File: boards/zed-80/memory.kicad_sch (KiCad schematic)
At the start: 6 parts, among them U3 TT74LS32BI, U5 AT28C256-15PU, U7 HM628128BLP-10

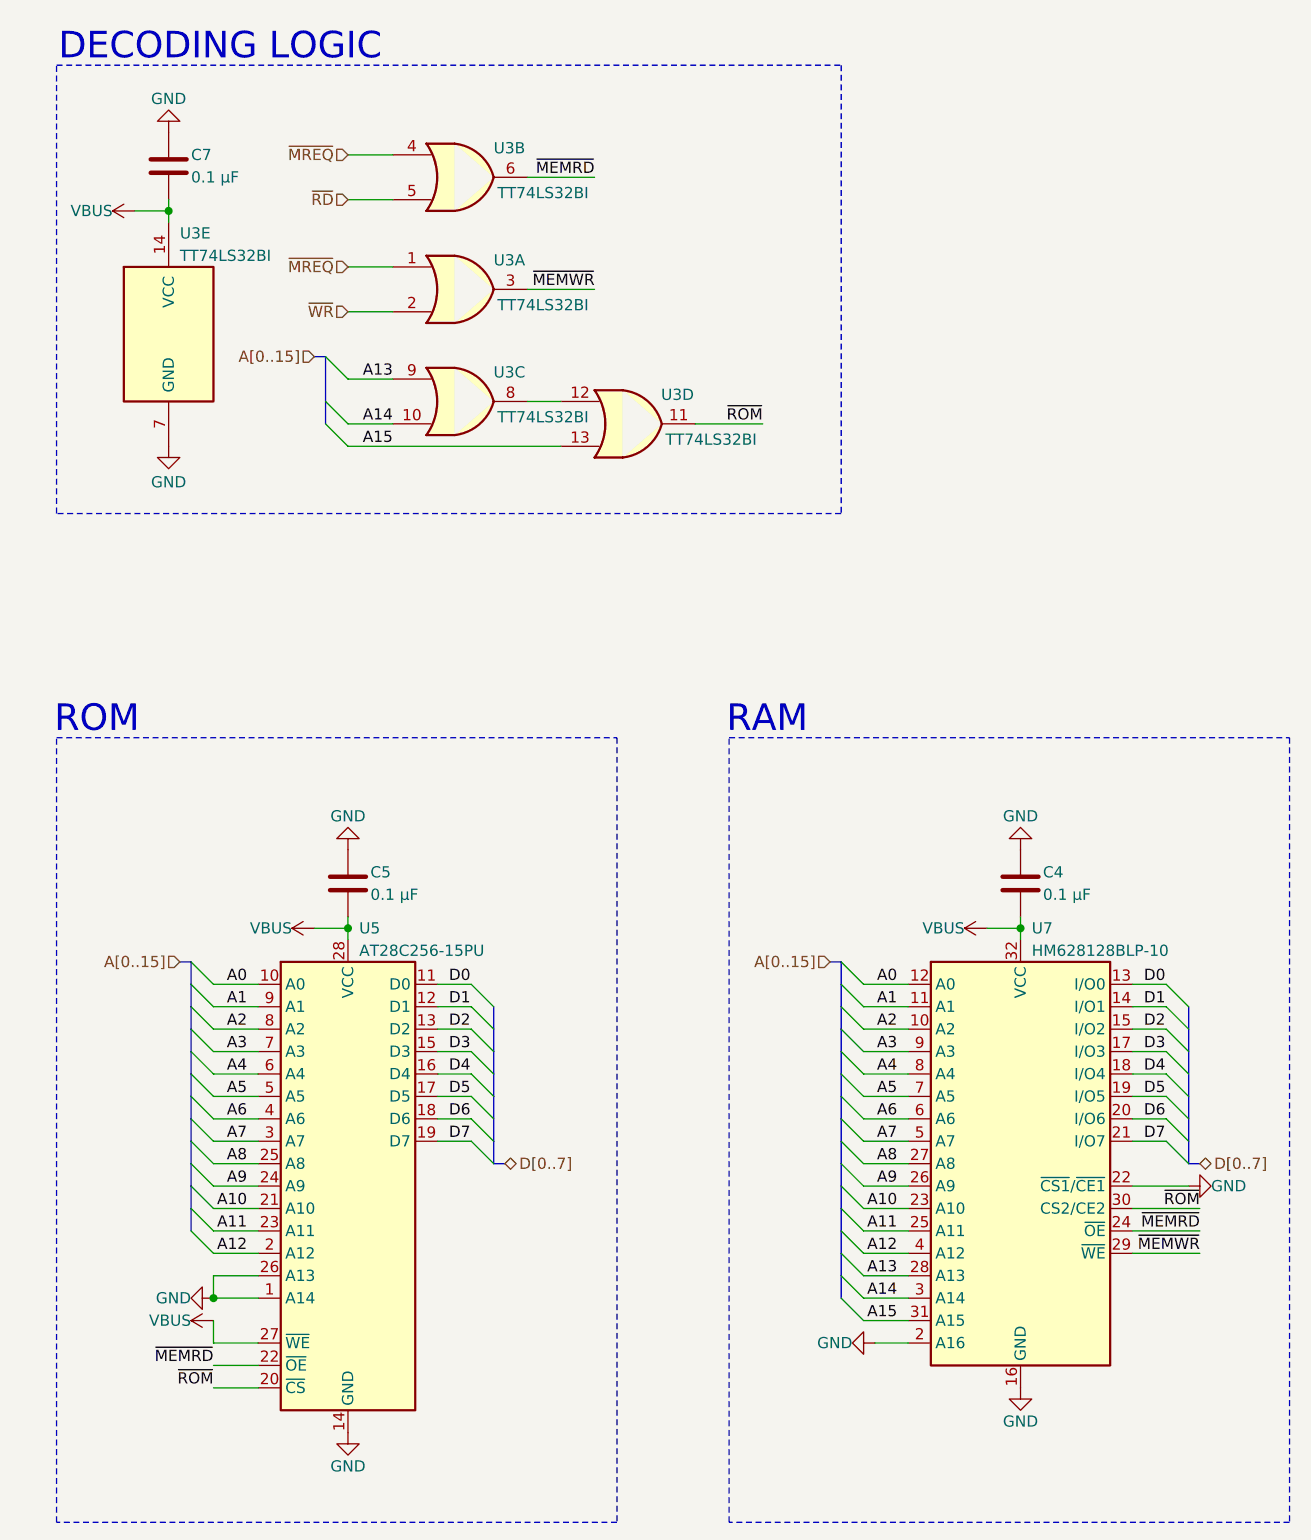
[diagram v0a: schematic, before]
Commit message: Polished schematics and basic PCB setup
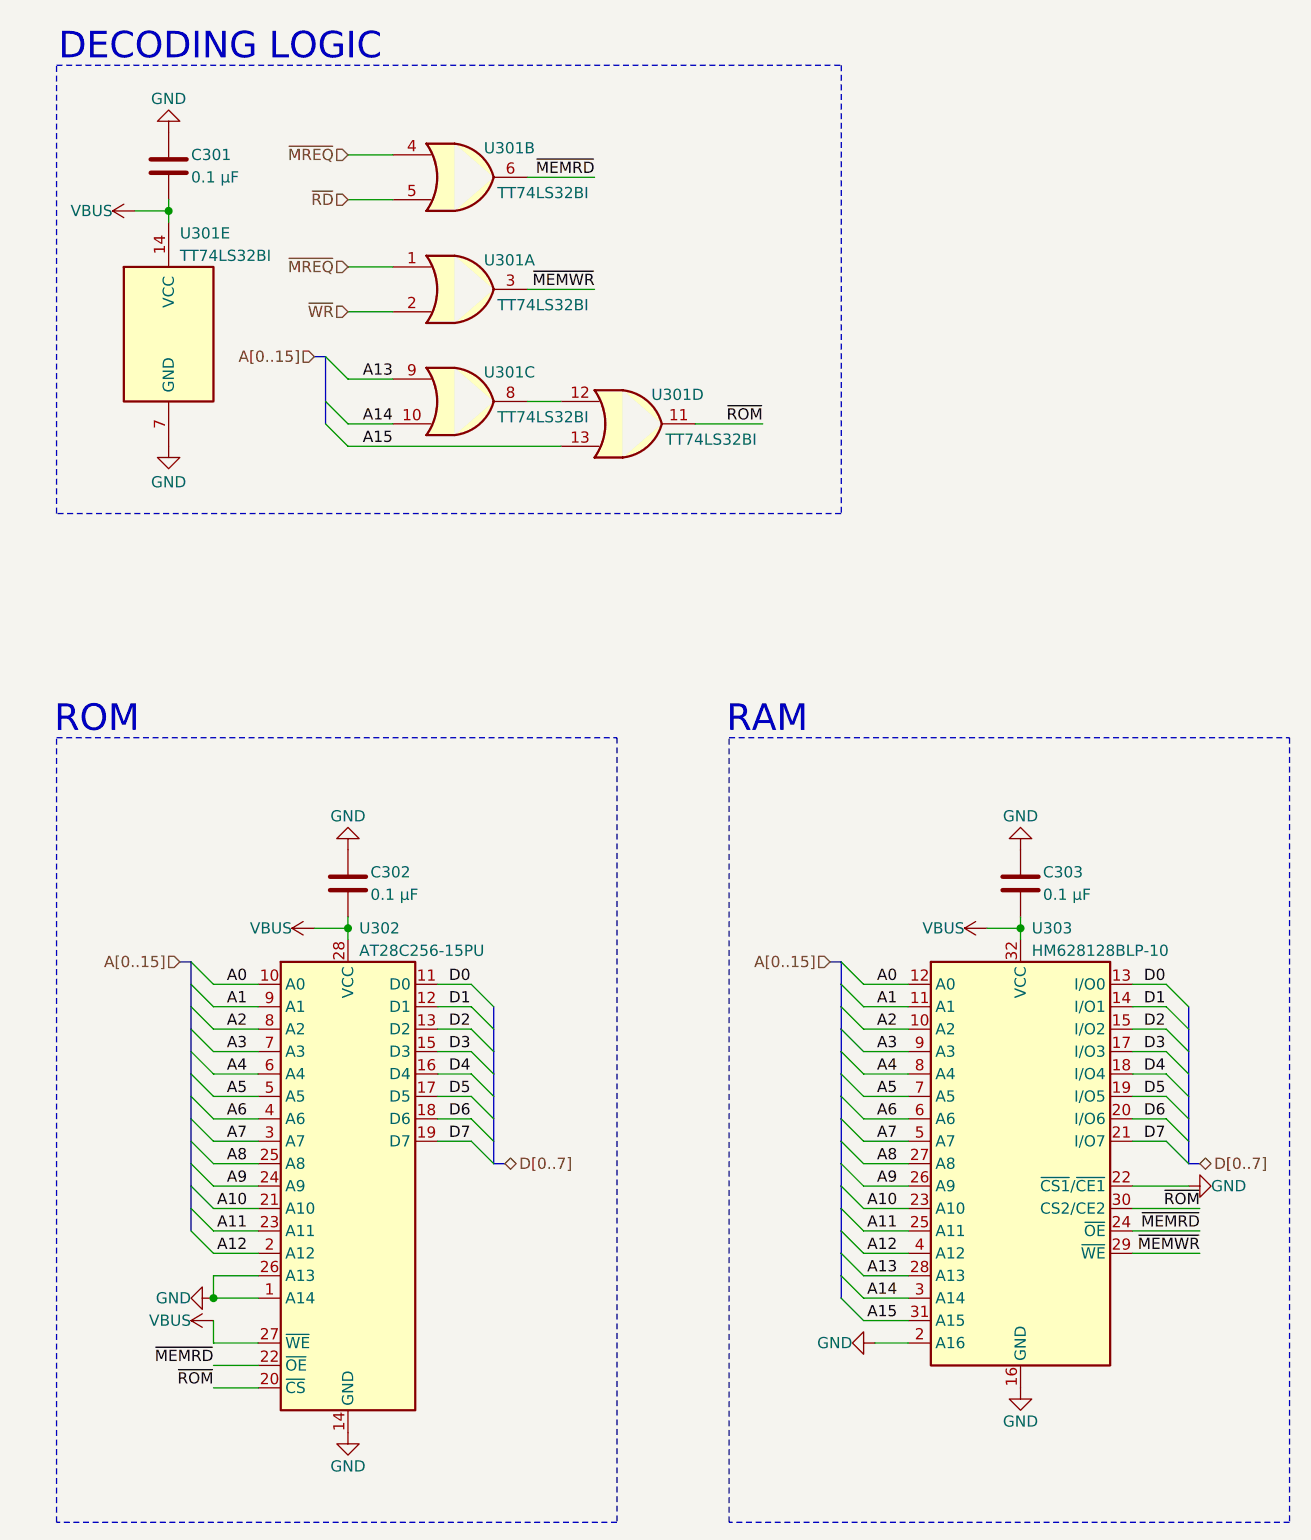
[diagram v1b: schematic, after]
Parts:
- renumbered C7 to C301, C5 to C302, C4 to C303, U3 to U301, U5 to U302, U7 to U303
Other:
- company: (none) -> Dragos Bajanica
- title: (none) -> Memory
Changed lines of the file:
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@@
 	(generator_version "9.0")
 	(paper "A4")
+	(title_block
+		(title "Memory")
+		(date "2025-12-31")
+		(rev "A")
+		(company "Dragos Bajanica")
+	)
 	(rectangle
 		(start 25.4 25.4)
@@
 		(on_board yes)
 		(dnp no)
-		(property "Reference" "#PWR04"
+		(property "Reference" "#PWR0310"
 			(at 134.62 123.19 0)
 			(effects
@@
 			(project "zed-80"
 				(path "/3141ac47-310a-4fc3-ab78-4d4b51ab76a4/5947d7ea-a932-40b2-8c9a-417fed404f71"
-					(reference "#PWR04")
+					(reference "#PWR0310")
 					(unit 1)
 				)
@@
 		(on_board yes)
 		(dnp no)
-		(property "Reference" "#PWR024"
+		(property "Reference" "#PWR0313"
 			(at 160.02 152.4 0)
 			(effects
@@
 			(project "zed-80"
 				(path "/3141ac47-310a-4fc3-ab78-4d4b51ab76a4/5947d7ea-a932-40b2-8c9a-417fed404f71"
-					(reference "#PWR024")
+					(reference "#PWR0313")
 					(unit 1)
 				)
@@
 		(on_board yes)
 		(dnp no)
-		(property "Reference" "#PWR023"
+		(property "Reference" "#PWR0309"
 			(at 111.76 170.18 0)
 			(effects
@@
 			(project "zed-80"
 				(path "/3141ac47-310a-4fc3-ab78-4d4b51ab76a4/5947d7ea-a932-40b2-8c9a-417fed404f71"
-					(reference "#PWR023")
+					(reference "#PWR0309")
 					(unit 1)
 				)
@@
 		(on_board yes)
 		(dnp no)
-		(property "Reference" "#PWR022"
+		(property "Reference" "#PWR0312"
 			(at 134.62 181.61 0)
 			(effects
@@
 			(project "zed-80"
 				(path "/3141ac47-310a-4fc3-ab78-4d4b51ab76a4/5947d7ea-a932-40b2-8c9a-417fed404f71"
-					(reference "#PWR022")
+					(reference "#PWR0312")
 					(unit 1)
 				)
@@
 		(on_board yes)
 		(dnp no)
-		(property "Reference" "C5"
+		(property "Reference" "C302"
 			(at 60.96 116.84 0)
 			(effects
@@
 			(project "zed-80"
 				(path "/3141ac47-310a-4fc3-ab78-4d4b51ab76a4/5947d7ea-a932-40b2-8c9a-417fed404f71"
-					(reference "C5")
+					(reference "C302")
 					(unit 1)
 				)
@@
 		(on_board yes)
 		(dnp no)
-		(property "Reference" "U3"
+		(property "Reference" "U301"
 			(at 76.708 34.798 0)
 			(effects
@@
 			(project "zed-80"
 				(path "/3141ac47-310a-4fc3-ab78-4d4b51ab76a4/5947d7ea-a932-40b2-8c9a-417fed404f71"
-					(reference "U3")
+					(reference "U301")
 					(unit 2)
 				)
@@
 		(on_board yes)
 		(dnp no)
-		(property "Reference" "U3"
+		(property "Reference" "U301"
 			(at 76.708 60.198 0)
 			(effects
@@
 			(project "zed-80"
 				(path "/3141ac47-310a-4fc3-ab78-4d4b51ab76a4/5947d7ea-a932-40b2-8c9a-417fed404f71"
-					(reference "U3")
+					(reference "U301")
 					(unit 3)
 				)
@@
 		(on_board yes)
 		(dnp no)
-		(property "Reference" "#PWR05"
+		(property "Reference" "#PWR0307"
 			(at 58.42 107.95 0)
 			(effects
@@
 			(project "zed-80"
 				(path "/3141ac47-310a-4fc3-ab78-4d4b51ab76a4/5947d7ea-a932-40b2-8c9a-417fed404f71"
-					(reference "#PWR05")
+					(reference "#PWR0307")
 					(unit 1)
 				)
@@
 		(on_board yes)
 		(dnp no)
-		(property "Reference" "#PWR033"
+		(property "Reference" "#PWR0304"
 			(at 36.83 165.1 0)
 			(effects
@@
 			(project "zed-80"
 				(path "/3141ac47-310a-4fc3-ab78-4d4b51ab76a4/5947d7ea-a932-40b2-8c9a-417fed404f71"
-					(reference "#PWR033")
+					(reference "#PWR0304")
 					(unit 1)
 				)
@@
 		(on_board yes)
 		(dnp no)
-		(property "Reference" "#PWR020"
+		(property "Reference" "#PWR0303"
 			(at 38.1 74.93 0)
 			(effects
@@
 			(project "zed-80"
 				(path "/3141ac47-310a-4fc3-ab78-4d4b51ab76a4/5947d7ea-a932-40b2-8c9a-417fed404f71"
-					(reference "#PWR020")
+					(reference "#PWR0303")
 					(unit 1)
 				)
@@
 		(on_board yes)
 		(dnp no)
-		(property "Reference" "U5"
+		(property "Reference" "U302"
 			(at 59.69 123.19 0)
 			(effects
@@
 			(project "zed-80"
 				(path "/3141ac47-310a-4fc3-ab78-4d4b51ab76a4/5947d7ea-a932-40b2-8c9a-417fed404f71"
-					(reference "U5")
+					(reference "U302")
 					(unit 1)
 				)
@@
 		(on_board yes)
 		(dnp no)
-		(property "Reference" "U3"
+		(property "Reference" "U301"
 			(at 95.758 62.738 0)
 			(effects
@@
 			(project "zed-80"
 				(path "/3141ac47-310a-4fc3-ab78-4d4b51ab76a4/5947d7ea-a932-40b2-8c9a-417fed404f71"
-					(reference "U3")
+					(reference "U301")
 					(unit 4)
 				)
@@
 		(on_board yes)
 		(dnp no)
-		(property "Reference" "#PWR09"
+		(property "Reference" "#PWR0301"
 			(at 38.1 41.91 0)
 			(effects
@@
 			(project "zed-80"
 				(path "/3141ac47-310a-4fc3-ab78-4d4b51ab76a4/5947d7ea-a932-40b2-8c9a-417fed404f71"
-					(reference "#PWR09")
+					(reference "#PWR0301")
 					(unit 1)
 				)
@@
 		(on_board yes)
 		(dnp no)
-		(property "Reference" "U3"
+		(property "Reference" "U301"
 			(at 76.708 47.498 0)
 			(effects
@@
 			(project "zed-80"
 				(path "/3141ac47-310a-4fc3-ab78-4d4b51ab76a4/5947d7ea-a932-40b2-8c9a-417fed404f71"
-					(reference "U3")
+					(reference "U301")
 					(unit 1)
 				)
@@
 		(on_board yes)
 		(dnp no)
-		(property "Reference" "C4"
+		(property "Reference" "C303"
 			(at 137.16 116.84 0)
 			(effects
@@
 			(project "zed-80"
 				(path "/3141ac47-310a-4fc3-ab78-4d4b51ab76a4/5947d7ea-a932-40b2-8c9a-417fed404f71"
-					(reference "C4")
+					(reference "C303")
 					(unit 1)
 				)
@@
 		(on_board yes)
 		(dnp no)
-		(property "Reference" "#PWR021"
+		(property "Reference" "#PWR0308"
 			(at 58.42 186.69 0)
 			(effects
@@
 			(project "zed-80"
 				(path "/3141ac47-310a-4fc3-ab78-4d4b51ab76a4/5947d7ea-a932-40b2-8c9a-417fed404f71"
-					(reference "#PWR021")
+					(reference "#PWR0308")
 					(unit 1)
 				)
@@
 		(on_board yes)
 		(dnp no)
-		(property "Reference" "#PWR03"
+		(property "Reference" "#PWR0306"
 			(at 58.42 123.19 0)
 			(effects
@@
 			(project "zed-80"
 				(path "/3141ac47-310a-4fc3-ab78-4d4b51ab76a4/5947d7ea-a932-40b2-8c9a-417fed404f71"
-					(reference "#PWR03")
+					(reference "#PWR0306")
 					(unit 1)
 				)
@@
 		(on_board yes)
 		(dnp no)
-		(property "Reference" "#PWR025"
+		(property "Reference" "#PWR0305"
 			(at 46.99 167.64 0)
 			(effects
@@
 			(project "zed-80"
 				(path "/3141ac47-310a-4fc3-ab78-4d4b51ab76a4/5947d7ea-a932-40b2-8c9a-417fed404f71"
-					(reference "#PWR025")
+					(reference "#PWR0305")
 					(unit 1)
 				)
@@
 		(on_board yes)
 		(dnp no)
-		(property "Reference" "C7"
+		(property "Reference" "C301"
 			(at 40.64 35.56 0)
 			(effects
@@
 			(project "zed-80"
 				(path "/3141ac47-310a-4fc3-ab78-4d4b51ab76a4/5947d7ea-a932-40b2-8c9a-417fed404f71"
-					(reference "C7")
+					(reference "C301")
 					(unit 1)
 				)
@@
 		(on_board yes)
 		(dnp no)
-		(property "Reference" "U7"
+		(property "Reference" "U303"
 			(at 135.89 123.19 0)
 			(effects
@@
 			(project "zed-80"
 				(path "/3141ac47-310a-4fc3-ab78-4d4b51ab76a4/5947d7ea-a932-40b2-8c9a-417fed404f71"
-					(reference "U7")
+					(reference "U303")
 					(unit 1)
 				)
@@
 		(on_board yes)
 		(dnp no)
-		(property "Reference" "#PWR010"
+		(property "Reference" "#PWR0302"
 			(at 38.1 26.67 0)
 			(effects
@@
 			(project "zed-80"
 				(path "/3141ac47-310a-4fc3-ab78-4d4b51ab76a4/5947d7ea-a932-40b2-8c9a-417fed404f71"
-					(reference "#PWR010")
+					(reference "#PWR0302")
 					(unit 1)
 				)
@@
 		(on_board yes)
 		(dnp no)
-		(property "Reference" "#PWR06"
+		(property "Reference" "#PWR0311"
 			(at 134.62 107.95 0)
 			(effects
@@
 			(project "zed-80"
 				(path "/3141ac47-310a-4fc3-ab78-4d4b51ab76a4/5947d7ea-a932-40b2-8c9a-417fed404f71"
-					(reference "#PWR06")
+					(reference "#PWR0311")
 					(unit 1)
 				)
@@
 		(on_board yes)
 		(dnp no)
-		(property "Reference" "U3"
+		(property "Reference" "U301"
 			(at 39.37 44.45 0)
 			(effects
@@
 			(project "zed-80"
 				(path "/3141ac47-310a-4fc3-ab78-4d4b51ab76a4/5947d7ea-a932-40b2-8c9a-417fed404f71"
-					(reference "U3")
+					(reference "U301")
 					(unit 5)
 				)

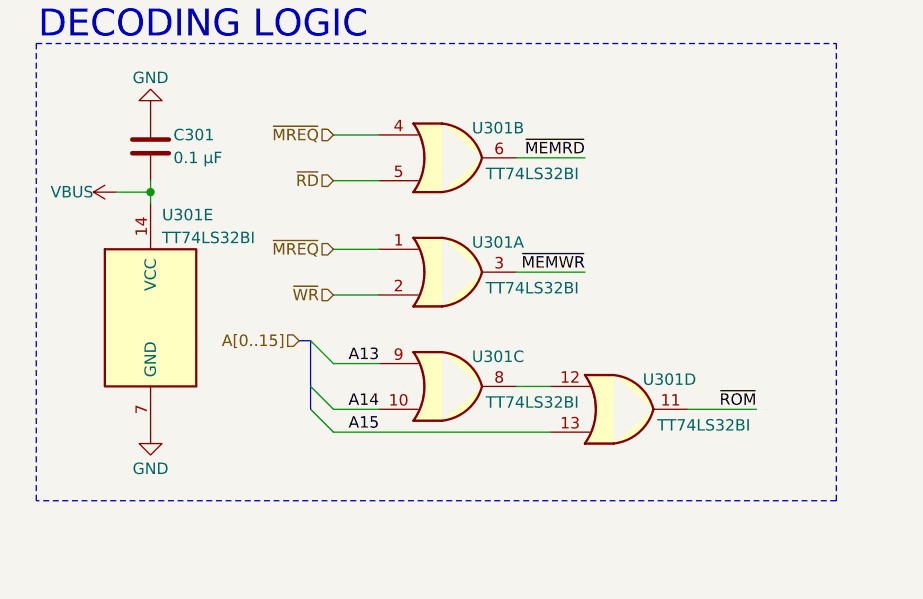
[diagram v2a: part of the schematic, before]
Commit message: Fixed clock oscillator circuit
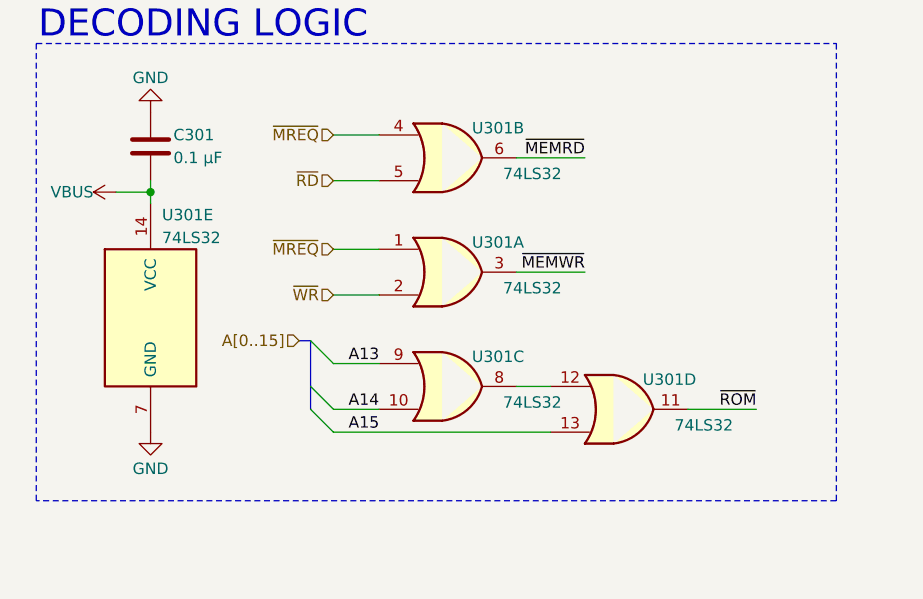
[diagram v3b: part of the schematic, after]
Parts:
- U301: value TT74LS32BI -> 74LS32
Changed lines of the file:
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@@
 	(title_block
 		(title "Memory")
-		(date "2026-01-01")
-		(rev "B")
+		(date "2026-03-17")
+		(rev "C")
 		(company "Dragos Bajanica")
 	)
@@
 			)
 		)
-		(property "Value" "TT74LS32BI"
+		(property "Value" "74LS32"
 			(at 80.518 39.878 0)
 			(effects
@@
 			)
 		)
-		(property "Value" "TT74LS32BI"
+		(property "Value" "74LS32"
 			(at 80.518 65.278 0)
 			(effects
@@
 			)
 		)
-		(property "Value" "TT74LS32BI"
+		(property "Value" "74LS32"
 			(at 99.568 67.818 0)
 			(effects
@@
 			)
 		)
-		(property "Value" "TT74LS32BI"
+		(property "Value" "74LS32"
 			(at 80.518 52.578 0)
 			(effects
@@
 			)
 		)
-		(property "Value" "TT74LS32BI"
+		(property "Value" "74LS32"
 			(at 39.37 46.99 0)
 			(effects
